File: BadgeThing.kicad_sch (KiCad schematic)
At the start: 65 parts, among them J1 USB_C_Receptacle_USB2.0, J2 Connector_Generic_Conn_01x02, J3 Ext 5V, J4 SWD Header, J6 Conn_01x07, J7 Conn_01x07, J8 Conn_01x08, SW1 BOOTSEL, SW2 ESP RESET, SW3 Left, SW4 Down, SW5 Select, SW6 Up, SW7 Right, U2 W25Q32JVSS, U3 RP2040, U4 NCP1117-3.3_SOT223, U5 ESP-12F, Y1 12.000MHz

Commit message: more routing + layout
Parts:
- D6: value Greeen -> Green
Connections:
- net +3V3: no longer D2.1 (VDD), D3.1 (VDD), D4.1 (VDD), D5.1 (VDD)
- net +5V: now also D2.1 (VDD), D3.1 (VDD), D4.1 (VDD), D5.1 (VDD)
- net BTN1: now also U3.36 (GPIO24); no longer U3.9 (GPIO7)
- net BTN2: now also U3.35 (GPIO23); no longer U3.11 (GPIO8)
- net BTN3: now also U3.34 (GPIO22); no longer U3.12 (GPIO9)
- net BTN4: now also U3.32 (GPIO21); no longer U3.13 (GPIO10)
- net BTN5: now also U3.31 (GPIO20); no longer U3.14 (GPIO11)
- net CS1: now also U3.30 (GPIO19); no longer U3.7 (GPIO5)
- net DC: now also U3.28 (GPIO17); no longer U3.2 (GPIO0)
- net ESP12: no longer U5.6 (GPIO12)
- net ESP13: no longer U5.7 (GPIO13)
- net ESP14: no longer U5.5 (GPIO14)
- net ESP15: no longer U5.16 (GPIO15)
- net ESP16: no longer U5.4 (GPIO16)
- net ESP2: no longer U5.17 (GPIO2)
- net ESP4: no longer U5.19 (GPIO4)
- net ESP5: no longer U5.20 (GPIO5)
- net GP15: no longer U3.18 (GPIO15)
- net GP16: no longer U3.27 (GPIO16)
- net GP17: no longer U3.28 (GPIO17)
- net GP18: no longer U3.29 (GPIO18)
- net GP19: no longer U3.30 (GPIO19)
- net GP20: no longer U3.31 (GPIO20)
- net GP21: no longer U3.32 (GPIO21)
- net GP22: no longer U3.34 (GPIO22)
- net GP23: no longer U3.35 (GPIO23)
- net GP24: no longer U3.36 (GPIO24)
- net GP26: no longer U3.38 (GPIO26_ADC0)
- net GP27: no longer U3.39 (GPIO27_ADC1)
- net GP28: no longer U3.40 (GPIO28_ADC2)
- net GP29: no longer U3.41 (GPIO29_ADC3)
- net MISO: now also U3.27 (GPIO16); no longer U3.6 (GPIO4)
- net MOSI: now also U3.18 (GPIO15); no longer U3.5 (GPIO3)
- net RST: now also U3.29 (GPIO18); no longer U3.3 (GPIO1)
- net SCLK: now also U3.17 (GPIO14); no longer U3.4 (GPIO2)
- net WS2812B: no longer U3.17 (GPIO14)

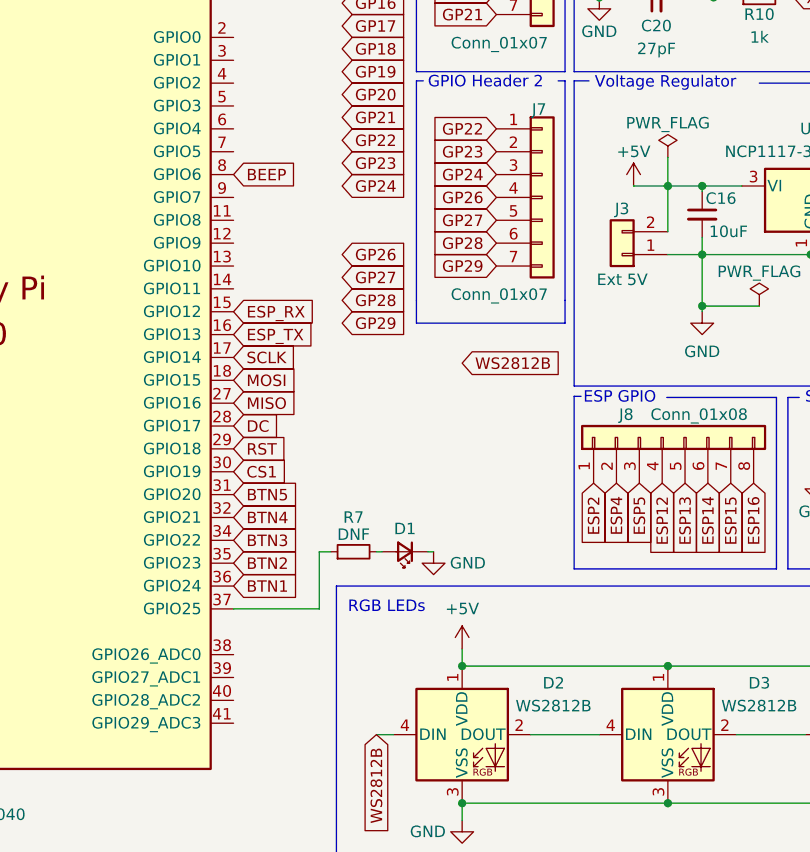
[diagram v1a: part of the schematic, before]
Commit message: Completed initial routing
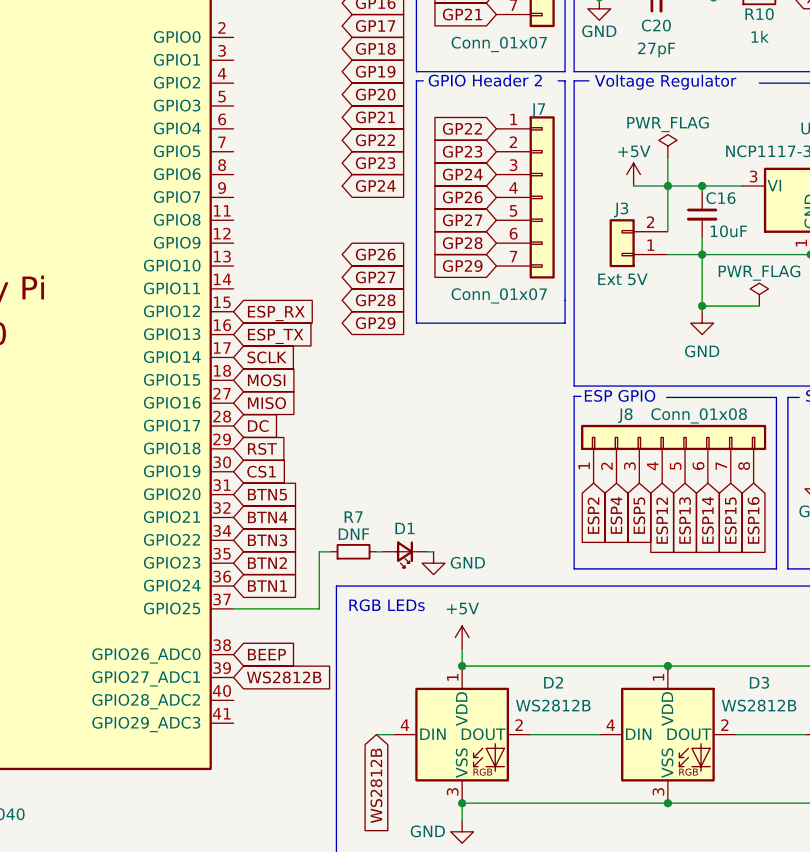
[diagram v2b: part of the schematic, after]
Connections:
- net BEEP: now also U3.38 (GPIO26_ADC0); no longer U3.8 (GPIO6)
- net WS2812B: now also U3.39 (GPIO27_ADC1)
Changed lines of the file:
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@@
     )
   )
-  (global_label "WS2812B" (shape input) (at 179.07 94.615 0) (fields_autoplaced)
-    (effects (font (size 1.27 1.27)) (justify left))
-    (property "Intersheetrefs" "${INTERSHEET_REFS}" (at 190.7447 94.615 0)
+  (global_label "WS2812B" (shape input) (at 153.67 129.54 0) (fields_autoplaced)
+    (effects (font (size 1.27 1.27)) (justify left))
+    (property "Intersheetrefs" "${INTERSHEET_REFS}" (at 165.3447 129.54 0)
       (effects (font (size 1.27 1.27)) (justify left) hide)
     )
@@
     )
   )
-  (global_label "BEEP" (shape input) (at 153.67 73.66 0) (fields_autoplaced)
-    (effects (font (size 1.27 1.27)) (justify left))
-    (property "Intersheetrefs" "${INTERSHEET_REFS}" (at 161.4138 73.66 0)
-      (effects (font (size 1.27 1.27)) (justify left) hide)
-    )
-  )
   (global_label "SWCLK" (shape input) (at 90.17 123.19 180) (fields_autoplaced)
     (effects (font (size 1.27 1.27)) (justify right))
@@
     )
   )
+  (global_label "BEEP" (shape input) (at 153.67 127 0) (fields_autoplaced)
+    (effects (font (size 1.27 1.27)) (justify left))
+    (property "Intersheetrefs" "${INTERSHEET_REFS}" (at 161.4138 127 0)
+      (effects (font (size 1.27 1.27)) (justify left) hide)
+    )
+  )

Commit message: Layout tweaks + JLC part numbers
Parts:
- removed D6: Green, LED_SMD:LED_0402_1005Metric_Pad0.77x0.64mm_HandSolder, symbol Device:LED_Small
- C6: LCSC (none) -> C15525
- D1: LCSC (none) -> C2297
- R1, R13, R14: LCSC (none) -> C25744
- U5: LCSC (none) -> C82898
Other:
- note removed: "ABLS-12.000MHZ-B4-T"
- note removed: "Power LED"
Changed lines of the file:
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@@
     (stroke (width 0) (type default))
   )
-  (polyline (pts (xy 238.125 84.455) (xy 219.075 84.455))
-    (stroke (width 0) (type default))
-  )
   (polyline (pts (xy 238.125 98.425) (xy 238.125 117.475))
     (stroke (width 0) (type default))
@@
     (stroke (width 0) (type default))
   )
-  (wire (pts (xy 222.885 90.17) (xy 226.06 90.17))
-    (stroke (width 0) (type default))
-  )
   (wire (pts (xy 203.2 43.18) (xy 207.01 43.18))
     (stroke (width 0) (type default))
@@
     (stroke (width 0) (type default))
   )
-  (polyline (pts (xy 219.075 84.455) (xy 219.075 97.155))
-    (stroke (width 0) (type default))
-  )
   (wire (pts (xy 138.43 19.05) (xy 142.24 19.05))
     (stroke (width 0) (type default))
@@
     (stroke (width 0) (type default))
   )
-  (wire (pts (xy 231.14 90.17) (xy 234.315 90.17))
-    (stroke (width 0) (type default))
-  )
   (polyline (pts (xy 215.265 98.425) (xy 216.535 98.425))
     (stroke (width 0) (type default))
@@
     (effects (font (size 1.27 1.27)) (justify left bottom))
   )
-  (text "ABLS-12.000MHZ-B4-T" (at 203.2 41.275 0)
-    (effects (font (size 1 1)) (justify left bottom))
-  )
   (text "ICSP" (at 67.183 136.779 0)
     (effects (font (size 1.27 1.27)) (justify left bottom))
@@
     (effects (font (size 1.27 1.27)) (justify left bottom))
   )
-  (text "Power LED" (at 219.71 86.995 0)
-    (effects (font (size 1.27 1.27)) (justify left bottom))
-  )
   (text "Crystal" (at 193.802 35.814 0)
     (effects (font (size 1.27 1.27)) (justify left bottom))
@@
       (effects (font (size 1.27 1.27)) hide)
     )
+    (property "LCSC" "C25744" (at 64.77 111.125 0)
+      (effects (font (size 1.27 1.27)) hide)
+    )
     (pin "1")
     (pin "2")
@@
       (effects (font (size 1.27 1.27)) hide)
     )
+    (property "LCSC" "C25744" (at 66.675 111.125 0)
+      (effects (font (size 1.27 1.27)) hide)
+    )
     (pin "1")
     (pin "2")
@@
       (effects (font (size 1.27 1.27)) hide)
     )
+    (property "LCSC" "C25744" (at 28.575 51.435 0)
+      (effects (font (size 1.27 1.27)) hide)
+    )
     (pin "1")
     (pin "2")
@@
       (effects (font (size 1.27 1.27)) hide)
     )
+    (property "LCSC" "C15525" (at 27.94 91.44 0)
+      (effects (font (size 1.27 1.27)) hide)
+    )
     (pin "1")
     (pin "2")
@@
       (effects (font (size 1.27 1.27)) hide)
     )
+    (property "LCSC" "C2297" (at 172.72 115.57 0)
+      (effects (font (size 1.27 1.27)) hide)
+    )
     (pin "1")
     (pin "2")
@@
     )
   )
-  (symbol (lib_id "power:+3V3") (at 234.315 90.17 0) (unit 1)
-    (in_bom yes) (on_board yes) (dnp no) (fields_autoplaced)
-    (property "Reference" "#PWR044" (at 234.315 93.98 0)
-      (effects (font (size 1.27 1.27)) hide)
-    )
-    (property "Value" "+3V3" (at 234.315 86.36 0)
-      (effects (font (size 1.27 1.27)))
-    )
-    (property "Footprint" "" (at 234.315 90.17 0)
-      (effects (font (size 1.27 1.27)) hide)
-    )
-    (property "Datasheet" "" (at 234.315 90.17 0)
-      (effects (font (size 1.27 1.27)) hide)
-    )
-    (pin "1")
-    (instances
-      (project "BadgeThing"
-        (path "/35d5f6bf-e39e-48ab-813a-17587fce37db"
-          (reference "#PWR044") (unit 1)
-        )
-      )
-    )
-  )
   (symbol (lib_id "power:GND") (at 28.575 54.61 0) (unit 1)
     (in_bom yes) (on_board yes) (dnp no)
@@
       (effects (font (size 1.27 1.27)) hide)
     )
+    (property "LCSC" "C82898" (at 40.64 128.905 0)
+      (effects (font (size 1.27 1.27)) hide)
+    )
     (pin "1")
     (pin "10")
@@
     )
   )
-  (symbol (lib_id "Device:LED_Small") (at 228.6 90.17 0) (unit 1)
-    (in_bom yes) (on_board yes) (dnp no)
-    (property "Reference" "D6" (at 228.6 92.71 0)
-      (effects (font (size 1.27 1.27)))
-    )
-    (property "Value" "Green" (at 227.33 94.615 0)
-      (effects (font (size 1.27 1.27)) (justify left))
-    )
-    (property "Footprint" "LED_SMD:LED_0402_1005Metric_Pad0.77x0.64mm_HandSolder" (at 228.6 90.17 90)
-      (effects (font (size 1.27 1.27)) hide)
-    )
-    (property "Datasheet" "~" (at 228.6 90.17 90)
-      (effects (font (size 1.27 1.27)) hide)
-    )
-    (pin "1")
-    (pin "2")
-    (instances
-      (project "BadgeThing"
-        (path "/35d5f6bf-e39e-48ab-813a-17587fce37db"
-          (reference "D6") (unit 1)
-        )
-      )
-    )
-  )
   (symbol (lib_id "power:GND") (at 205.74 88.9 0) (unit 1)
     (in_bom yes) (on_board yes) (dnp no)
@@
         )
       )
-    )
-  )
-  (symbol (lib_id "power:GND") (at 222.885 90.17 0) (unit 1)
-    (in_bom yes) (on_board yes) (dnp no)
-    (property "Reference" "#PWR043" (at 222.885 96.52 0)
-      (effects (font (size 1.27 1.27)) hide)
-    )
-    (property "Value" "GND" (at 222.885 94.615 0)
-      (effects (font (size 1.27 1.27)))
-    )
-    (property "Footprint" "" (at 222.885 90.17 0)
-      (effects (font (size 1.27 1.27)) hide)
-    )
-    (property "Datasheet" "" (at 222.885 90.17 0)
-      (effects (font (size 1.27 1.27)) hide)
-    )
-    (pin "1")
-    (instances
-      (project "BadgeThing"
-        (path "/35d5f6bf-e39e-48ab-813a-17587fce37db"
-          (reference "#PWR043") (unit 1)
-        )
-      )
-      (project "PicoLX"
-        (path "/c5e5d8b8-bebd-4318-85a6-adbafb95dd10"
-          (reference "#PWR016") (unit 1)
-        )
-      )
-      (project "Panel"
-        (path "/f55927e3-6490-4e79-9229-dceeb24f0064"
-          (reference "#PWR015") (unit 1)
-        )
-      )

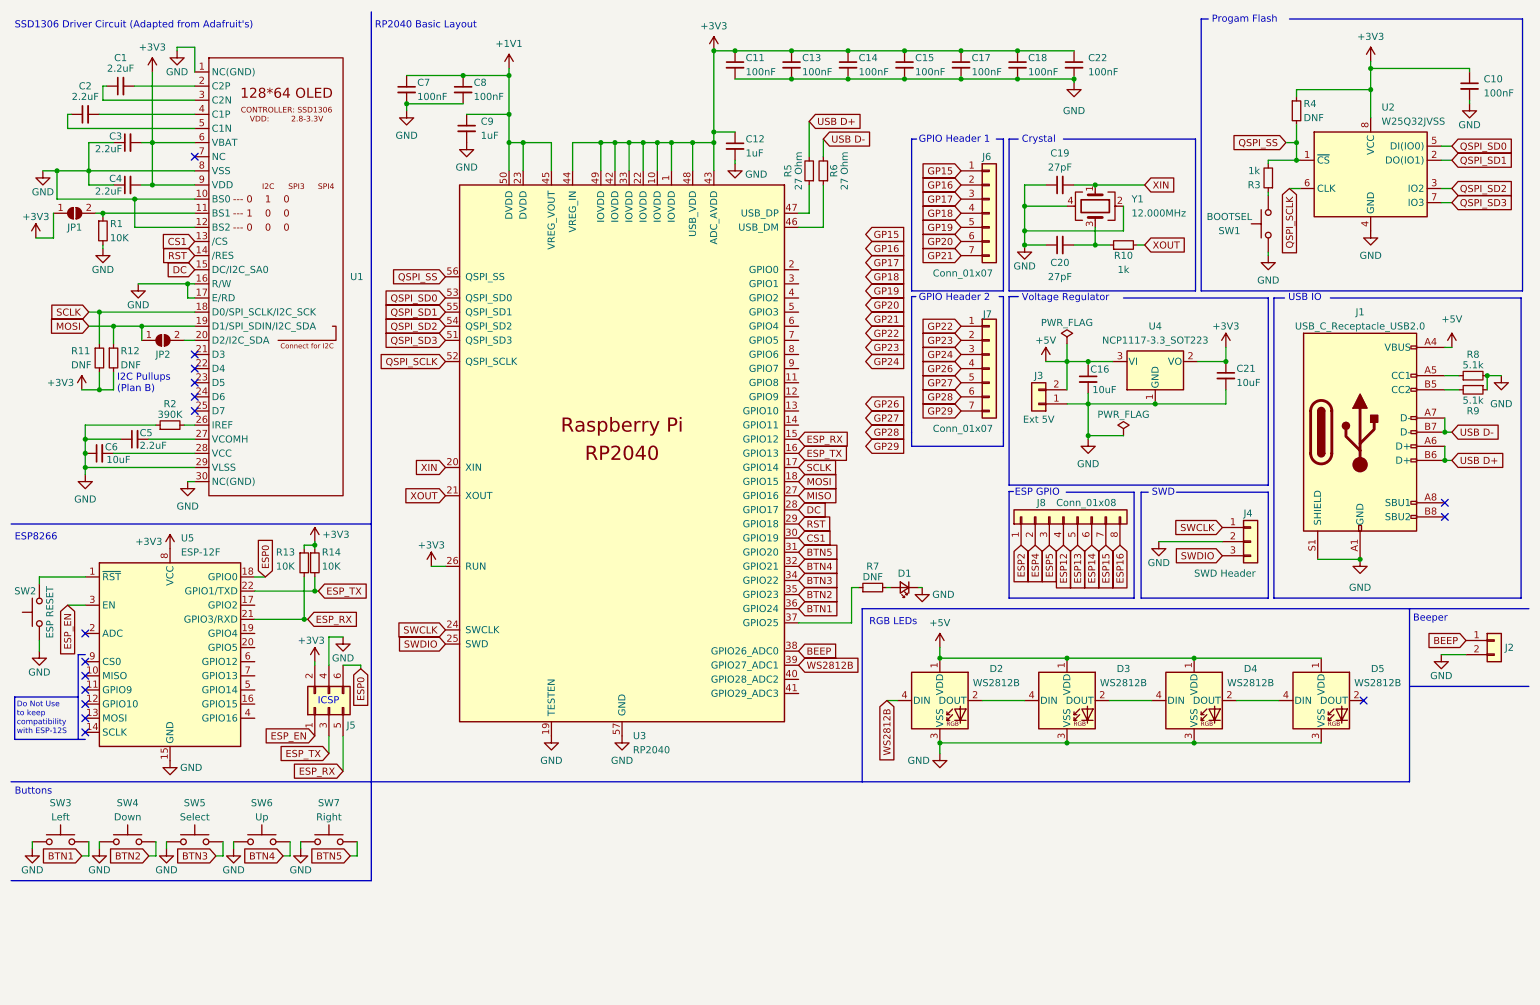
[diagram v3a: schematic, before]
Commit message: Final board layout, up to first production order
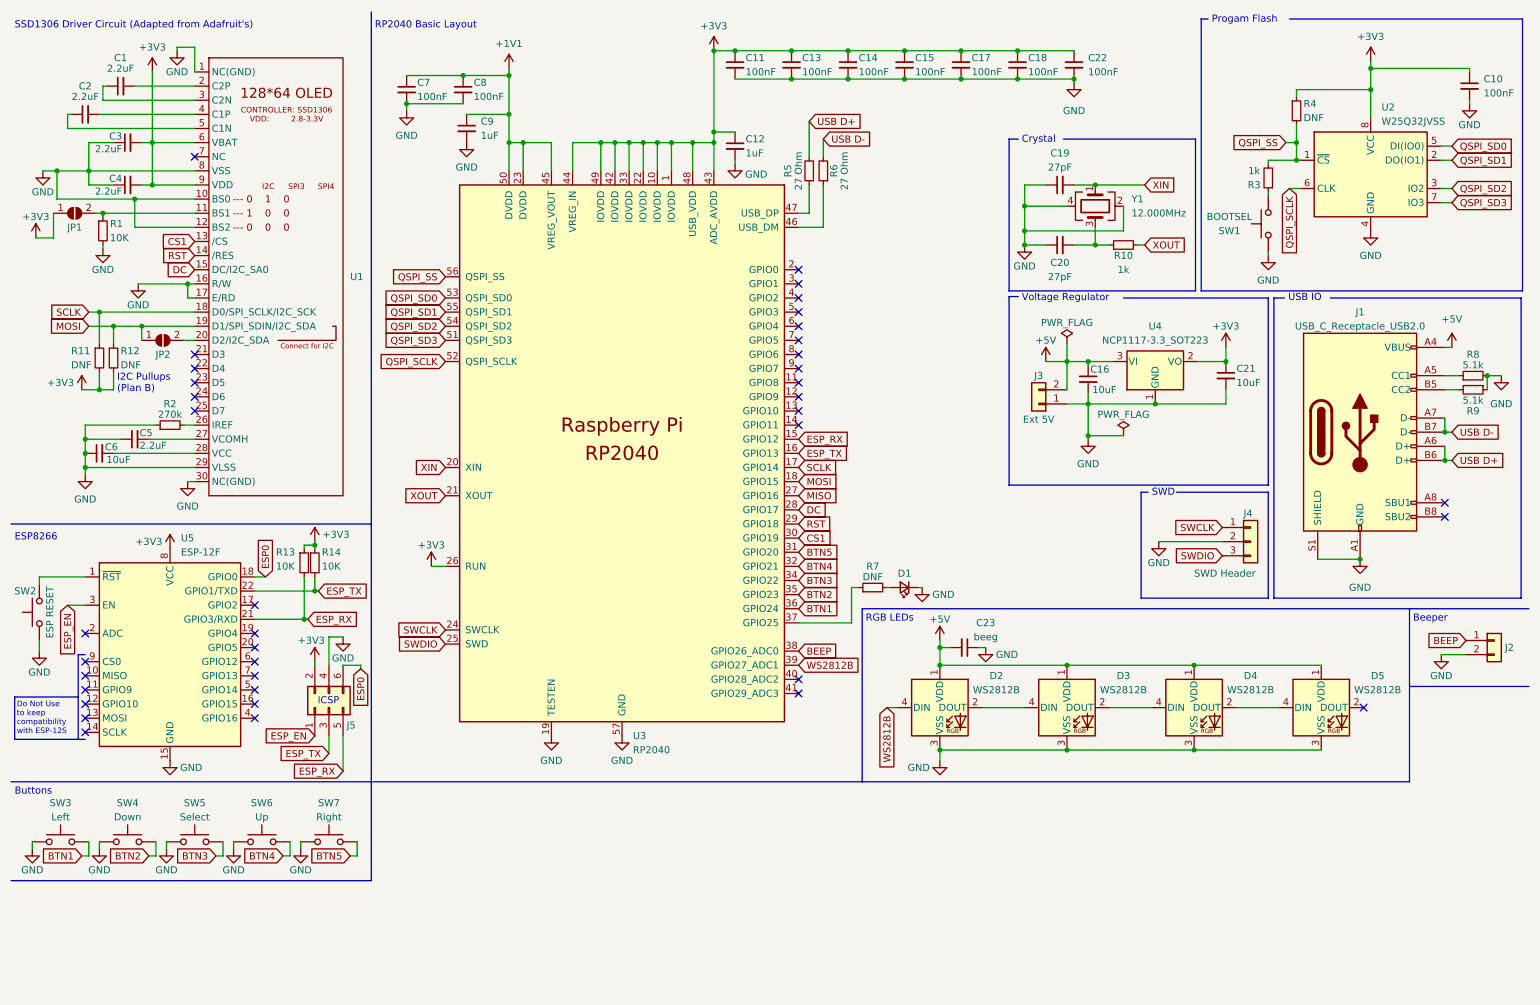
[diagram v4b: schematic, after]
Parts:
- removed J6, J7: Conn_01x07, Connector_PinHeader_2.54mm:PinHeader_1x07_P2.54mm_Vertical, symbol Connector_Generic:Conn_01x07
- removed J8: Conn_01x08, Connector_PinHeader_2.54mm:PinHeader_1x08_P2.54mm_Vertical, symbol Connector_Generic:Conn_01x08
- added C23: beeg, Capacitor_SMD:C_0402_1005Metric_Pad0.74x0.62mm_HandSolder, symbol Device:C_Small
- D2, D3, D4, D5: LCSC (none) -> C2761795
- R10, R3: LCSC C106235 -> C11702
- R11, R12, R4: LCSC (none) -> C25744
- R2: value 390K -> 270k; LCSC (none) -> C25770
- R7: LCSC (none) -> C25091
- SW1: footprint Button_Switch_SMD:SW_Push_1P1T_NO_6x6mm_H9.5mm -> Button_Switch_SMD:SW_Push_1P1T_XKB_TS-1187A
- SW2: footprint Button_Switch_SMD:SW_Push_1P1T_NO_6x6mm_H9.5mm -> Button_Switch_SMD:SW_Push_1P1T_XKB_TS-1187A; LCSC (none) -> C318884
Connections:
- net +5V: now also C23.2
- net GND: now also C23.1
- no-connect marks 16 -> 38
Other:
- note removed: "ESP GPIO"
- note removed: "GPIO Header 1"
- note removed: "GPIO Header 2"
- moved on the sheet: D2, D3, D4, D5

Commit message: 3V3 input + small tweaks
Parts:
- added J6: External 3V3, Connector_PinHeader_2.54mm:PinHeader_1x02_P2.54mm_Vertical, symbol Connector_Generic:Conn_01x02
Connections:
- net +3V3: now also J6.2 (Pin_2)
- net GND: now also J6.1 (Pin_1)
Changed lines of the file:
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@@
   (junction (at 205.74 74.93) (diameter 0) (color 0 0 0 0)
   )
+  (junction (at 230.505 82.55) (diameter 0) (color 0 0 0 0)
+  )
   (junction (at 27.94 66.04) (diameter 0) (color 0 0 0 0)
   )
@@
   (junction (at 142.24 19.05) (diameter 0) (color 0 0 0 0)
   )
+  (junction (at 227.965 74.93) (diameter 0) (color 0 0 0 0)
+  )
   (junction (at 205.74 88.265) (diameter 0) (color 0 0 0 0)
   )
@@
     (stroke (width 0) (type default))
   )
+  (wire (pts (xy 230.505 82.55) (xy 230.505 84.455))
+    (stroke (width 0) (type default))
+  )
   (wire (pts (xy 69.215 124.46) (xy 69.215 129.54))
     (stroke (width 0) (type default))
@@
     (stroke (width 0) (type default))
   )
-  (wire (pts (xy 225.425 74.93) (xy 230.505 74.93))
+  (wire (pts (xy 225.425 74.93) (xy 227.965 74.93))
     (stroke (width 0) (type default))
   )
@@
     (stroke (width 0) (type default))
   )
+  (wire (pts (xy 227.965 74.93) (xy 227.965 84.455))
+    (stroke (width 0) (type default))
+  )
   (wire (pts (xy 179.07 129.54) (xy 201.93 129.54))
     (stroke (width 0) (type default))
@@
     (stroke (width 0) (type default))
   )
+  (wire (pts (xy 227.965 74.93) (xy 230.505 74.93))
+    (stroke (width 0) (type default))
+  )
   (wire (pts (xy 243.205 26.035) (xy 256.54 26.035))
     (stroke (width 0) (type default))
@@
         )
       )
+    )
+  )
+  (symbol (lib_id "Connector_Generic:Conn_01x02") (at 230.505 89.535 270) (unit 1)
+    (in_bom yes) (on_board yes) (dnp no)
+    (property "Reference" "J6" (at 225.425 89.535 0)
+      (effects (font (size 1.27 1.27)))
+    )
+    (property "Value" "External 3V3" (at 229.235 92.075 90)
+      (effects (font (size 1.27 1.27)))
+    )
+    (property "Footprint" "Connector_PinHeader_2.54mm:PinHeader_1x02_P2.54mm_Vertical" (at 230.505 89.535 0)
+      (effects (font (size 1.27 1.27)) hide)
+    )
+    (property "Datasheet" "~" (at 230.505 89.535 0)
+      (effects (font (size 1.27 1.27)) hide)
+    )
+    (pin "1")
+    (pin "2")
+    (instances
+      (project "BadgeThing"
+        (path "/35d5f6bf-e39e-48ab-813a-17587fce37db"
+          (reference "J6") (unit 1)
+        )
+      )
